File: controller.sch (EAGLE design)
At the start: 26 parts, among them IC1 MEGA8-P, IC2 VREG-LM340, IC3 MAX6675, J1 ICSP, Q1 16.0Mhz

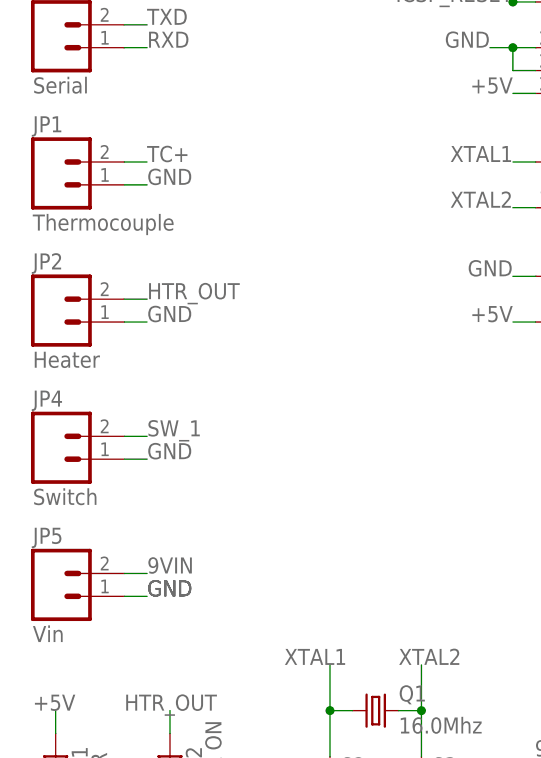
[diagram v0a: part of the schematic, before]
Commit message: Fixed orientation of screw terminals.
Screw terminals were oriented with receptacle facing inwards towards
the center of the board. Rotated them and performed some pin swaps.

Also added silk to label contrast trim pot on interface board.
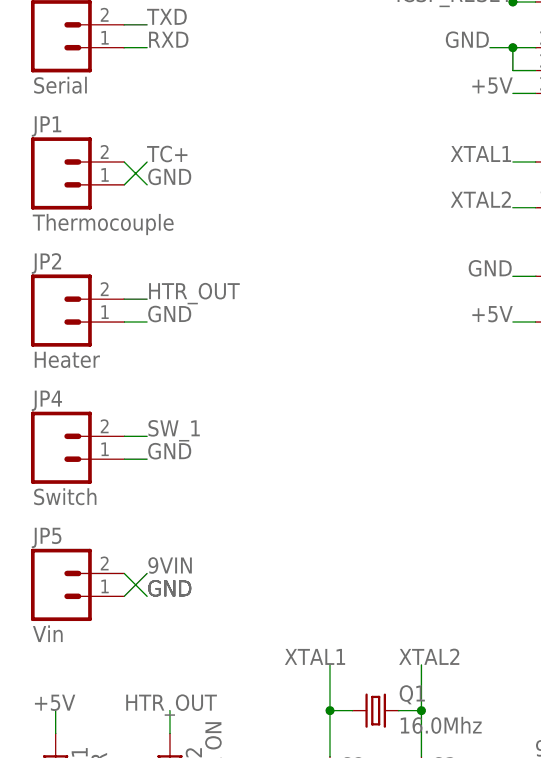
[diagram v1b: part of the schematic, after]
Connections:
- net 9VIN: now also JP5.1; no longer JP5.2
- net GND: now also JP1.2, JP5.2; no longer JP1.1, JP5.1
- net TC+: now also JP1.1; no longer JP1.2
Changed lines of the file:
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@@
 <setting verticaltext="up"/>
 </settings>
-<grid distance="0.1" unitdist="inch" unit="inch" style="lines" multiple="1" display="yes" altdistance="0.01" altunitdist="inch" altunit="inch"/>
+<grid distance="0.1" unitdist="inch" unit="inch" style="lines" multiple="1" display="no" altdistance="0.01" altunitdist="inch" altunit="inch"/>
 <layers>
 <layer number="1" name="Top" color="4" fill="1" visible="no" active="no"/>
@@
 </segment>
 <segment>
-<pinref part="JP1" gate="G$1" pin="1"/>
-<wire x1="12.7" y1="53.34" x2="15.24" y2="53.34" width="0.1524" layer="91"/>
+<pinref part="JP1" gate="G$1" pin="2"/>
+<wire x1="12.7" y1="55.88" x2="15.24" y2="53.34" width="0.1524" layer="91"/>
 <label x="15.24" y="53.34" size="1.778" layer="95"/>
 </segment>
@@
 </segment>
 <segment>
-<pinref part="JP5" gate="G$1" pin="1"/>
-<wire x1="12.7" y1="7.62" x2="15.24" y2="7.62" width="0.1524" layer="91"/>
+<pinref part="JP5" gate="G$1" pin="2"/>
+<wire x1="12.7" y1="10.16" x2="15.24" y2="7.62" width="0.1524" layer="91"/>
 <label x="15.24" y="7.62" size="1.778" layer="95"/>
 <label x="15.24" y="7.62" size="1.778" layer="95"/>
@@
 </segment>
 <segment>
-<pinref part="JP1" gate="G$1" pin="2"/>
-<wire x1="12.7" y1="55.88" x2="15.24" y2="55.88" width="0.1524" layer="91"/>
+<pinref part="JP1" gate="G$1" pin="1"/>
+<wire x1="12.7" y1="53.34" x2="15.24" y2="55.88" width="0.1524" layer="91"/>
 <label x="15.24" y="55.88" size="1.778" layer="95"/>
 </segment>
@@
 <net name="9VIN" class="1">
 <segment>
-<pinref part="JP5" gate="G$1" pin="2"/>
-<wire x1="12.7" y1="10.16" x2="15.24" y2="10.16" width="0.1524" layer="91"/>
+<pinref part="JP5" gate="G$1" pin="1"/>
+<wire x1="12.7" y1="7.62" x2="15.24" y2="10.16" width="0.1524" layer="91"/>
 <label x="15.24" y="10.16" size="1.778" layer="95"/>
 </segment>

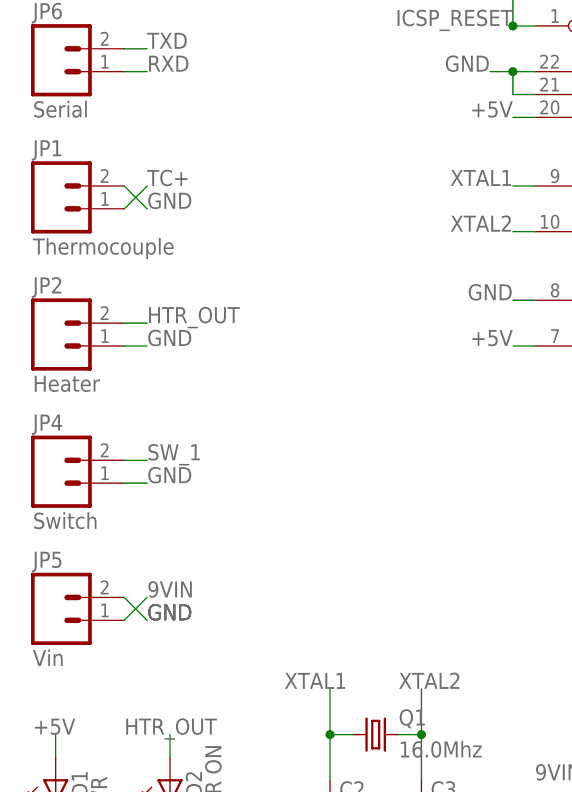
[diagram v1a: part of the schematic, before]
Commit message: Changed 1 of the aux power connectors to molex polarized header.
Made change for interface and for controller boards
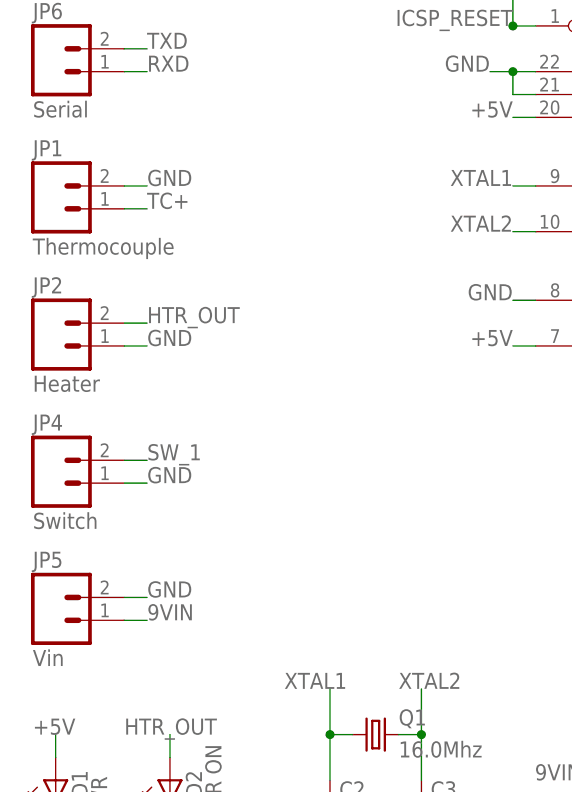
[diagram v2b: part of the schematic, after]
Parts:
- JP9: device SparkFun-Connectors:M02PTH -> SparkFun-Connectors:M02POLAR
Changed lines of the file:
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@@
 <part name="JP7" library="SparkFun-Connectors" deviceset="M02" device="PTH" value="I2C"/>
 <part name="JP8" library="SparkFun-Connectors" deviceset="M02" device="PTH" value="PWR_AUX"/>
-<part name="JP9" library="SparkFun-Connectors" deviceset="M02" device="PTH" value="PWR_AUX"/>
+<part name="JP9" library="SparkFun-Connectors" deviceset="M02" device="POLAR" value="PWR_AUX"/>
 </parts>
 <sheets>
@@
 <segment>
 <pinref part="JP1" gate="G$1" pin="2"/>
-<wire x1="12.7" y1="55.88" x2="15.24" y2="53.34" width="0.1524" layer="91"/>
-<label x="15.24" y="53.34" size="1.778" layer="95"/>
+<wire x1="12.7" y1="55.88" x2="15.24" y2="55.88" width="0.1524" layer="91"/>
+<label x="15.24" y="55.88" size="1.778" layer="95"/>
 </segment>
 <segment>
@@
 <segment>
 <pinref part="JP5" gate="G$1" pin="2"/>
-<wire x1="12.7" y1="10.16" x2="15.24" y2="7.62" width="0.1524" layer="91"/>
-<label x="15.24" y="7.62" size="1.778" layer="95"/>
-<label x="15.24" y="7.62" size="1.778" layer="95"/>
-<label x="15.24" y="7.62" size="1.778" layer="95"/>
+<wire x1="12.7" y1="10.16" x2="15.24" y2="10.16" width="0.1524" layer="91"/>
+<label x="15.24" y="10.16" size="1.778" layer="95"/>
 </segment>
 <segment>
@@
 <segment>
 <pinref part="JP1" gate="G$1" pin="1"/>
-<wire x1="12.7" y1="53.34" x2="15.24" y2="55.88" width="0.1524" layer="91"/>
-<label x="15.24" y="55.88" size="1.778" layer="95"/>
+<wire x1="12.7" y1="53.34" x2="15.24" y2="53.34" width="0.1524" layer="91"/>
+<label x="15.24" y="53.34" size="1.778" layer="95"/>
 </segment>
 </net>
@@
 <segment>
 <pinref part="JP5" gate="G$1" pin="1"/>
-<wire x1="12.7" y1="7.62" x2="15.24" y2="10.16" width="0.1524" layer="91"/>
-<label x="15.24" y="10.16" size="1.778" layer="95"/>
-</segment>
-<segment>
+<wire x1="12.7" y1="7.62" x2="15.24" y2="7.62" width="0.1524" layer="91"/>
+<label x="15.24" y="7.62" size="1.778" layer="95"/>
+</segment>
+<segment>

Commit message: Updated some layout, added logo
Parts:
- added U$1: MN-LOGO, Mikes-Aesthetics:MN-LOGO
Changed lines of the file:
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@@
 <part name="JP8" library="SparkFun-Connectors" deviceset="M02" device="PTH" value="PWR_AUX"/>
 <part name="JP9" library="SparkFun-Connectors" deviceset="M02" device="POLAR" value="PWR_AUX"/>
+<part name="U$1" library="Mikes-Aesthetics" deviceset="MN-LOGO" device=""/>
 </parts>
 <sheets>
@@
 <instance part="JP8" gate="G$1" x="5.08" y="99.06"/>
 <instance part="JP9" gate="G$1" x="27.94" y="99.06"/>
+<instance part="U$1" gate="G$1" x="198.12" y="-17.78"/>
 </instances>
 <busses>
